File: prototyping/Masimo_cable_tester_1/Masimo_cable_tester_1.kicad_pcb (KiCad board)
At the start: 2 copper layers, 28 parts, among them J1 Touchscreen HMI, J10 5V Jumper, J16 Debug Connections, J17 Banana Jack, J2 Conn_01x28_Socket, J3 Conn_01x28_Socket, J4 Barrel Jack 9V, J5 Conn_01x08, J6 SFML-110-02-L-D-A, J7 Conn_01x03_Pin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

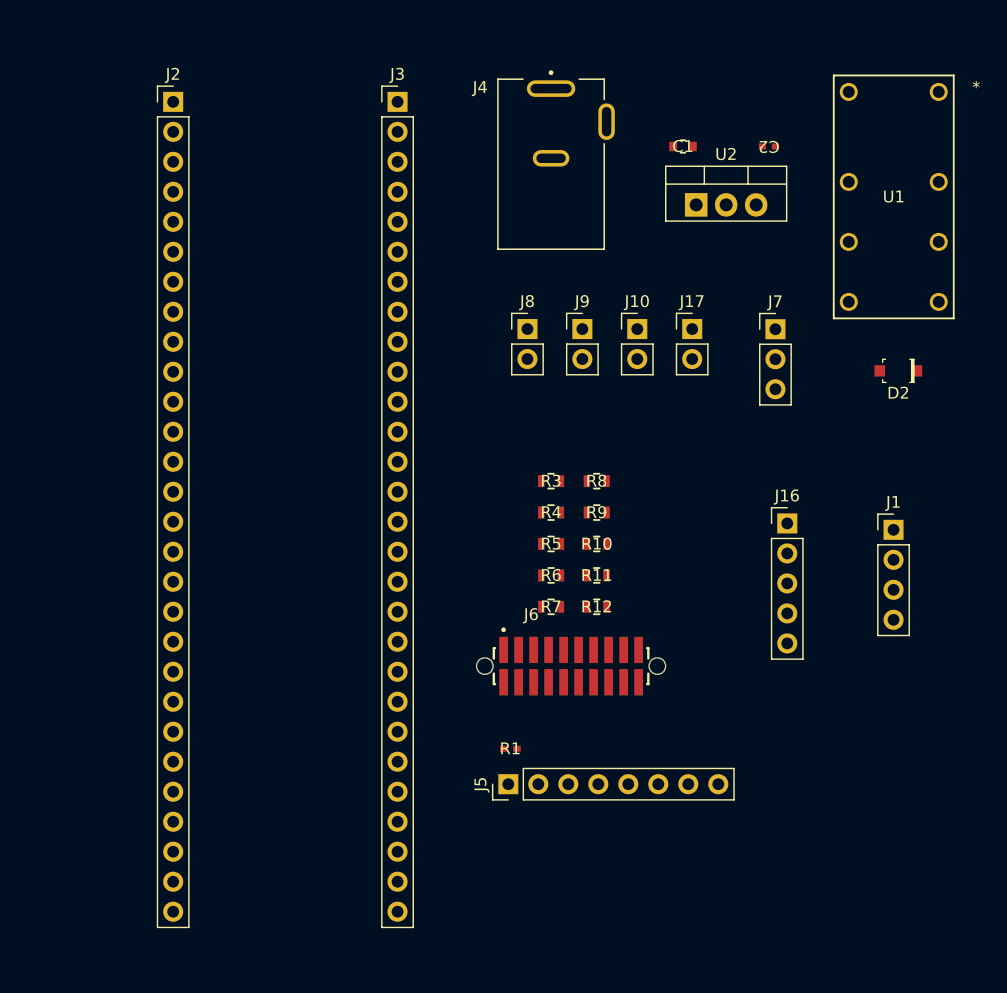
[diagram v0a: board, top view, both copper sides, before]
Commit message: Prototype Schematic and PCB Updates
Made a few changes to the schematic for ease of tracing on the PCB design. Started PCB layout of components, no traces yet
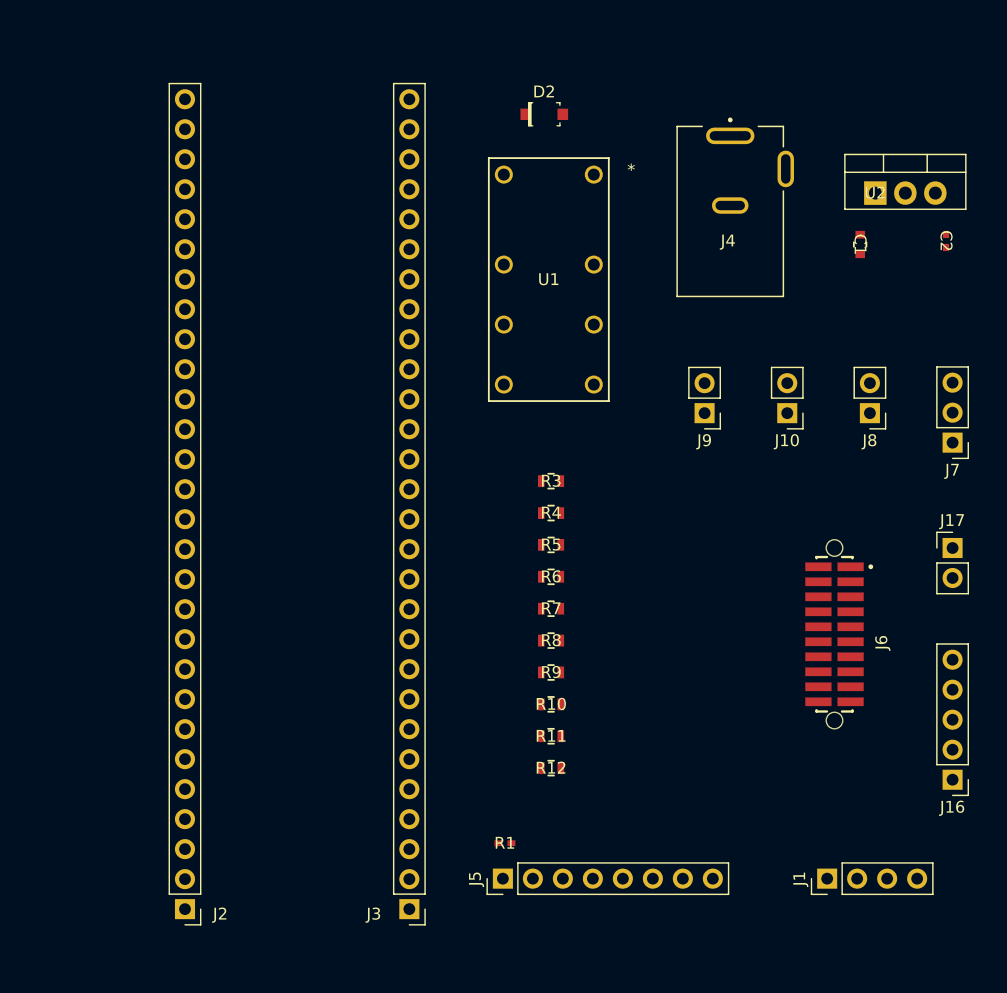
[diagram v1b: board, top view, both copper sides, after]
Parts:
- J10: value 5V Jumper -> MCU Board Power
- J2: value Conn_01x28_Socket -> Curiosity Nano AVR128DB48
- J5: value Conn_01x08 -> MicroSD PinHeader
- J7: value Conn_01x03_Pin -> HMI Power Toggle
- J8: value Jumper Pins 5V -> Board Power
- J9: value VOFF Jumper -> VOFF Toggle
- moved J2 68.4 mm to (94.0, 126.6), turned to 180 degrees
- moved J3 68.4 mm to (113.0, 126.6), turned to 180 degrees
- moved D2 37.0 mm to (124.4, 59.3), turned to 0 degrees
- moved J1 30.1 mm to (148.4, 124.0), turned to 90 degrees
- moved U1 30.0 mm to (121.0, 64.4)
- moved J8 29.9 mm to (152.0, 84.6), turned to 180 degrees
- moved J17 28.8 mm to (159.0, 96.0)
- moved J16 25.8 mm to (159.0, 115.6), turned to 180 degrees
- moved J6 22.5 mm to (149.0, 103.3), turned to -90 degrees
- moved J7 17.8 mm to (159.0, 87.1), turned to 180 degrees
- moved C1 17.1 mm to (151.2, 70.3), turned to -90 degrees
- moved C2 17.0 mm to (158.4, 70.0), turned to -90 degrees
- moved J4 15.7 mm to (140.2, 67.0)
- moved U2 15.2 mm to (152.5, 65.9)
- moved J10 14.6 mm to (145.0, 84.6), turned to 180 degrees
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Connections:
- J6 pad 01: ADC 1 -> unconnected-(J6-Pad01)
- J6 pad 02: ADC 6 -> ADC 1
- J6 pad 03: ADC 2 -> unconnected-(J6-Pad03)
- J6 pad 04: ADC 7 -> ADC 2
- J6 pad 05: ADC 3 -> unconnected-(J6-Pad05)
- J6 pad 06: ADC 8 -> ADC 3
- J6 pad 07: ADC 4 -> unconnected-(J6-Pad07)
- J6 pad 08: ADC 9 -> ADC 4
- J6 pad 09: ADC 5 -> unconnected-(J6-Pad09)
- J6 pad 10: ADC 10 -> ADC 5
- J6 pad 12: unconnected-(J6-Pad12) -> ADC 6
- J6 pad 14: unconnected-(J6-Pad14) -> ADC 7
- J6 pad 16: unconnected-(J6-Pad16) -> ADC 8
- J6 pad 18: unconnected-(J6-Pad18) -> ADC 9
- J6 pad 20: unconnected-(J6-Pad20) -> ADC 10

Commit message: Updated Prototype PCB Layout
Updated the prototype PCB layout. Tried optimizing placement of components for easier traces. Added an edge cut layer to made PCB 70mmx80mm
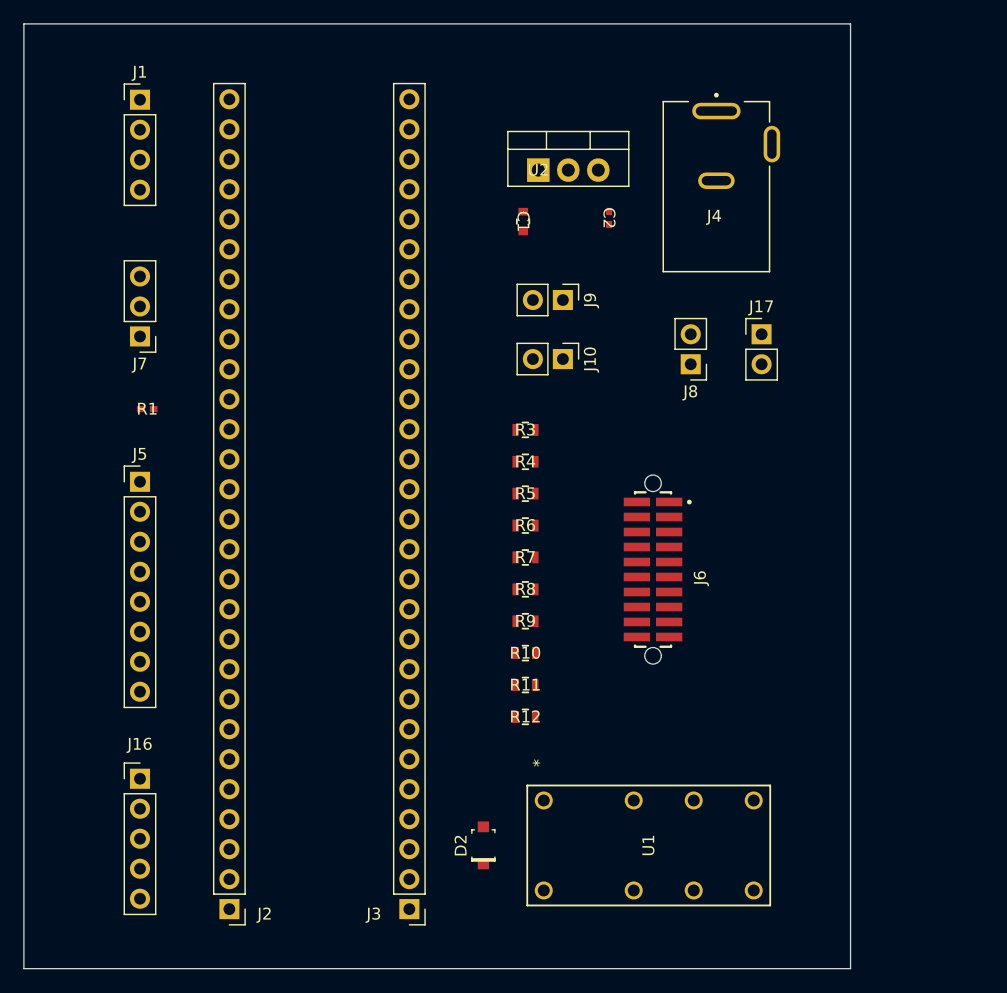
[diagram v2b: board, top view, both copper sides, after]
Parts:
- moved J1 88.0 mm to (90.2, 58.0), turned to 0 degrees
- moved J7 69.4 mm to (90.2, 78.1)
- moved J16 68.8 mm to (90.2, 115.5), turned to 0 degrees
- moved D2 62.1 mm to (119.3, 121.2), turned to 90 degrees
- moved U1 60.7 mm to (124.4, 125.0), turned to 90 degrees
- moved R1 47.6 mm to (90.8, 84.2)
- moved J5 45.5 mm to (90.2, 90.4), turned to 0 degrees
- moved C2 28.6 mm to (129.9, 68.1)
- moved C1 28.6 mm to (122.6, 68.4)
- moved U2 28.6 mm to (123.9, 64.0)
- moved J17 24.3 mm to (142.8, 77.9)
- moved J10 19.5 mm to (126.0, 80.0), turned to -90 degrees
- moved J6 16.3 mm to (133.6, 97.8)
- moved J8 15.7 mm to (136.8, 80.4)
- moved J9 15.4 mm to (126.0, 75.0), turned to -90 degrees
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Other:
- board outline added: 70 x 80 mm

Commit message: Layed traces down.
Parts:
- moved J2 68.6 mm to (97.8, 58.0), turned to 0 degrees
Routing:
- net GND: track 0.00 -> 59.6 mm
- net Net-(J8-Pin_2): track 0.00 -> 42.7 mm
- net CTRL 1: track 0.00 -> 24.0 mm
- net CTRL 2: track 0.00 -> 23.8 mm
- net CTRL 3: track 0.00 -> 23.7 mm
- net CTRL 4: track 0.00 -> 23.5 mm
- net 9V: track 0.00 -> 21.2 mm
- net RSig: track 0.00 -> 13.9 mm
- net ADC 10: track 0.00 -> 11.4 mm
- net ADC 1: track 0.00 -> 11.1 mm
- net ADC 9: track 0.00 -> 10.8 mm
- net ADC 2: track 0.00 -> 10.6 mm
- net ADC 8: track 0.00 -> 10.2 mm
- net ADC 3: track 0.00 -> 9.96 mm
- net ADC 7: track 0.00 -> 9.64 mm
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
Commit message: Update traces.
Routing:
- net GND: track 59.6 -> 16.9 mm
- net Net-(J8-Pin_2): track 42.7 -> 3.88 mm
- net 9V: track 21.2 -> 4.06 mm
- net RSig: track 13.9 -> 0.00 mm
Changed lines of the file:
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@@
 	)
 	(segment
-		(start 113 116.42)
-		(end 116.195 119.615)
-		(width 0.2)
-		(layer "F.Cu")
-		(net 1)
-	)
-	(segment
-		(start 136.715 61.8)
-		(end 143.7 61.8)
-		(width 0.2)
-		(layer "F.Cu")
-		(net 1)
-	)
-	(segment
-		(start 126.46 65.54)
-		(end 126.46 64)
-		(width 0.2)
-		(layer "F.Cu")
-		(net 1)
-	)
-	(segment
-		(start 129.9072 68.6078)
-		(end 126.46 65.1606)
-		(width 0.2)
-		(layer "F.Cu")
-		(net 1)
-	)
-	(segment
-		(start 122.6322 71.6322)
-		(end 126 75)
-		(width 0.2)
-		(layer "F.Cu")
-		(net 1)
-	)
-	(segment
-		(start 122.6322 69.1828)
-		(end 122.6322 71.6322)
-		(width 0.2)
-		(layer "F.Cu")
-		(net 1)
-	)
-	(segment
-		(start 122.8172 69.1828)
-		(end 126.46 65.54)
-		(width 0.2)
-		(layer "F.Cu")
-		(net 1)
-	)
-	(segment
-		(start 116.195 119.615)
-		(end 119.27 119.615)
-		(width 0.2)
-		(layer "F.Cu")
-		(net 1)
-	)
-	(segment
-		(start 97.76 116.42)
-		(end 113 116.42)
-		(width 0.2)
-		(layer "F.Cu")
-		(net 1)
-	)
-	(segment
-		(start 126.46 65.1606)
-		(end 126.46 64)
+		(start 122.745636 69.1828)
+		(end 122.6322 69.1828)
 		(width 0.2)
 		(layer "F.Cu")
@@
 	)
 	(segment
-		(start 128.92 59)
-		(end 139 59)
+		(start 136.715 61.8)
+		(end 143.7 61.8)
 		(width 0.2)
 		(layer "F.Cu")
-		(net 2)
+		(net 1)
 	)
 	(segment
@@
 	)
 	(segment
-		(start 123.92 64)
-		(end 128.92 59)
-		(width 0.2)
-		(layer "F.Cu")
-		(net 2)
-	)
-	(segment
-		(start 129 66.595)
-		(end 129.9072 67.5022)
+		(start 129.9072 67.5022)
+		(end 129.9072 64.9072)
 		(width 0.2)
 		(layer "F.Cu")
@@
 	)
 	(segment
-		(start 142.699 60.535372)
-		(end 143.285372 59.949)
+		(start 129.9072 64.9072)
+		(end 129 64)
 		(width 0.2)
 		(layer "F.Cu")
@@
 	)
 	(segment
-		(start 129 64)
-		(end 129 66.595)
-		(width 0.2)
-		(layer "F.Cu")
-		(net 3)
-	)
-	(segment
-		(start 144.114628 59.949)
-		(end 144.701 60.535372)
-		(width 0.2)
-		(layer "F.Cu")
-		(net 3)
-	)
-	(segment
-		(start 143.285372 59.949)
-		(end 144.114628 59.949)
-		(width 0.2)
-		(layer "F.Cu")
-		(net 3)
-	)
-	(segment
-		(start 144.701 70.0268)
-		(end 136.8278 77.9)
-		(width 0.2)
-		(layer "F.Cu")
-		(net 3)
-	)
-	(segment
-		(start 136.874028 60.535372)
-		(end 142.699 60.535372)
-		(width 0.2)
-		(layer "F.Cu")
-		(net 3)
-	)
-	(segment
-		(start 129.9072 67.5022)
-		(end 136.874028 60.535372)
-		(width 0.2)
-		(layer "F.Cu")
-		(net 3)
-	)
-	(segment
-		(start 144.701 60.535372)
-		(end 144.701 70.0268)
-		(width 0.2)
-		(layer "F.Cu")
-		(net 3)
-	)
-	(segment
-		(start 119.27 122.765)
-		(end 122.145 122.765)
-		(width 0.2)
-		(layer "F.Cu")
-		(net 4)
-	)
-	(segment
-		(start 113 118.96)
-		(end 116.805 122.765)
-		(width 0.2)
-		(layer "F.Cu")
-		(net 4)
-	)
-	(segment
-		(start 122.145 122.765)
-		(end 124.38 125)
-		(width 0.2)
-		(layer "F.Cu")
-		(net 4)
-	)
-	(segment
-		(start 116.805 122.765)
-		(end 119.27 122.765)
-		(width 0.2)
-		(layer "F.Cu")
-		(net 4)
-	)
-	(segment
